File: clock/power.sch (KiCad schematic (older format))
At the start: 47 parts, among them U501 TPS56428, U502 TPS56428, U503 TPS56428

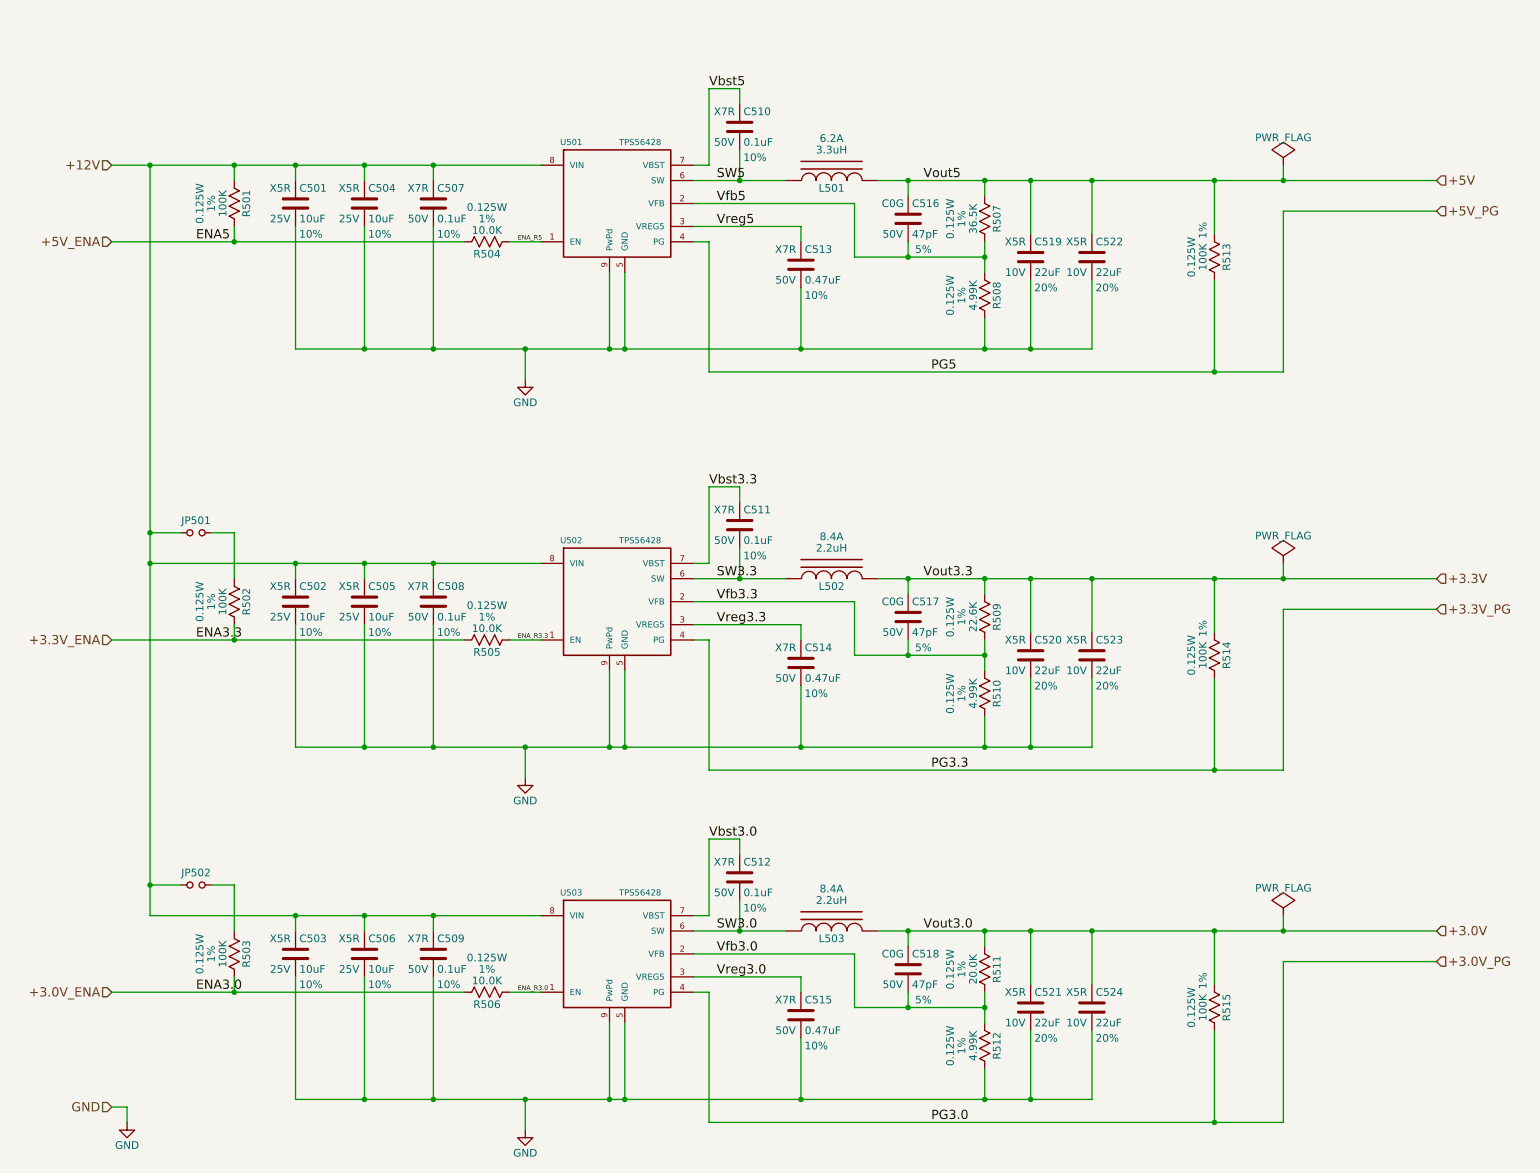
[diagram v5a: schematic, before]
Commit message: Preliminary changes from lab bring up.   Properly connect ref2 on PCA9306.   Duplicate +5V power good to drive +3.3V converter.   Change gain structure on OCXO control voltage drive.   Add FET control to disable linear regulators.
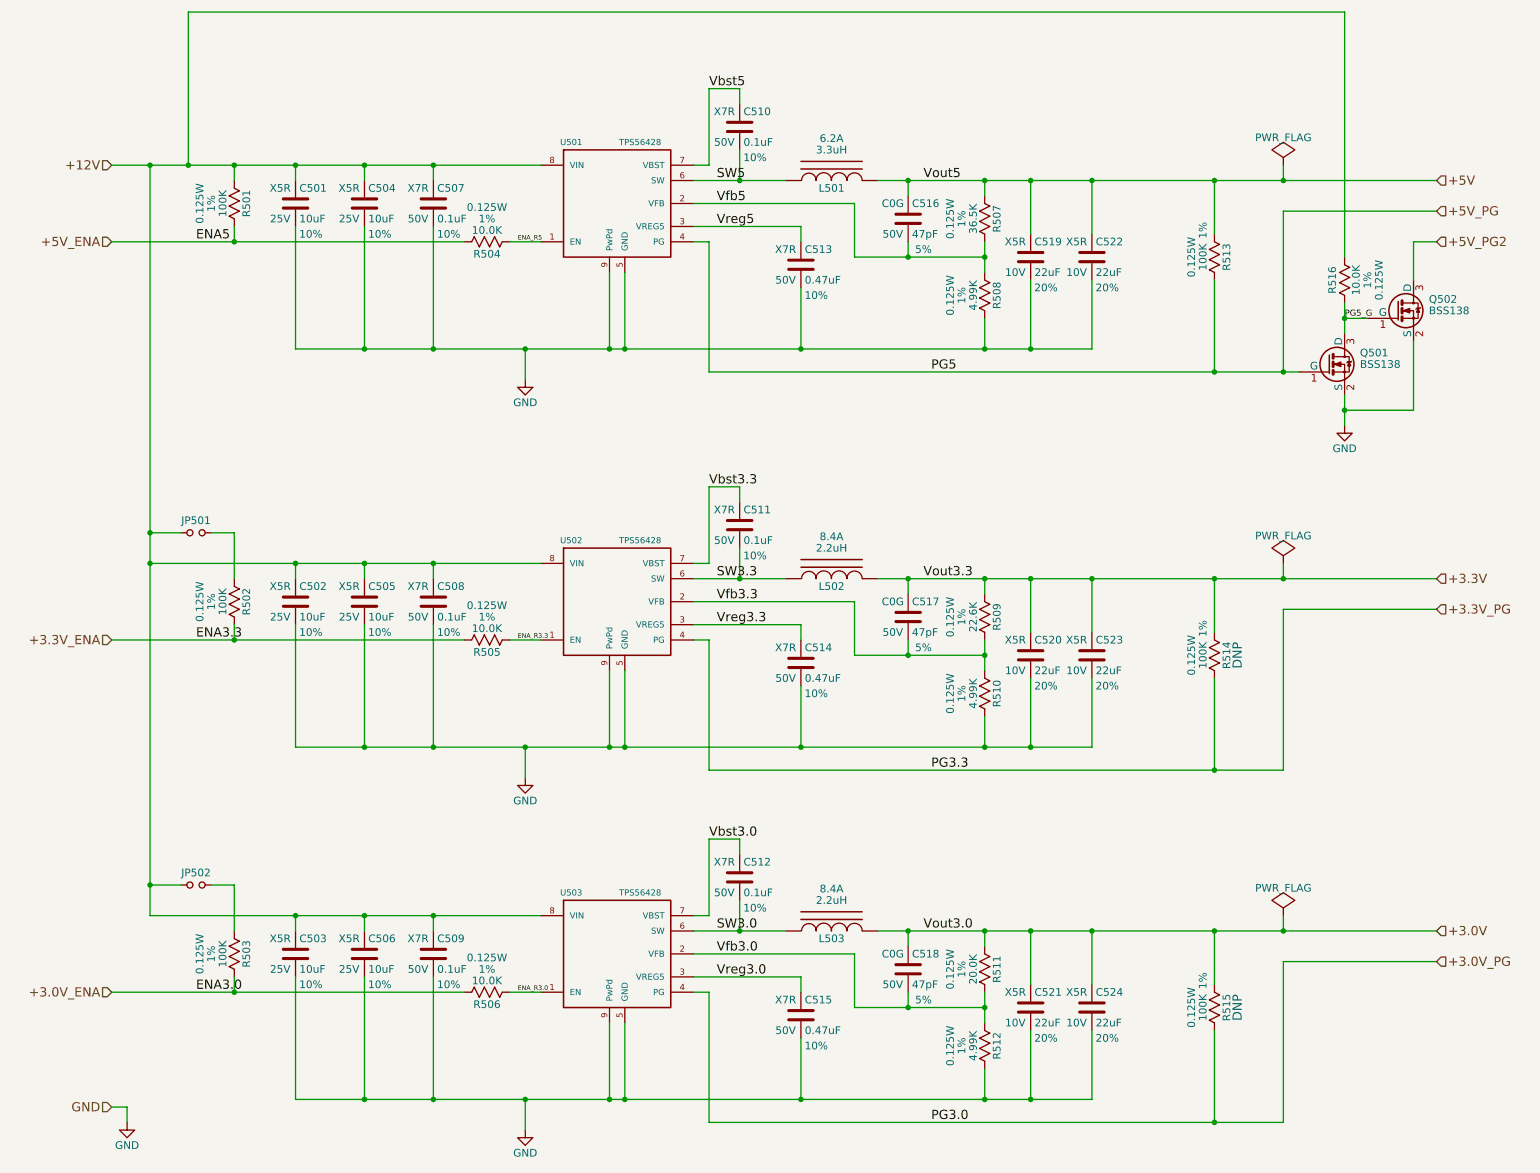
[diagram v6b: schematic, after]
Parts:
- added Q501, Q502: BSS138, local:SOT-23-3_NXP_HandSoldering, symbol BSS138
- added R516: 10.0K, Resistors_SMD:R_0805_HandSoldering, symbol R_local
- R514, R515: DNP (none) -> DNP
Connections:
- net +12V: now also R516.2
- net +5V_PG: now also Q501.1 (G)
- net GND: now also Q501.2 (S), Q502.2 (S)
- new net +5V_PG2: Q502.3 (D)
- new net PG5_G: Q501.3 (D), Q502.1 (G), R516.1
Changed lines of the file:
@@
 	3500 2750 5800 2750
 Wire Wire Line
-	7400 3600 11150 3600
+	7400 3600 11250 3600
 Wire Wire Line
 	6850 3450 6850 2950
@@
 Connection ~ 4300 2750
 $Comp
-L GND #PWR071
+L GND #PWR502
 U 1 1 55FF67B4
 P 6200 3650
-F 0 "#PWR071" H 6200 3400 50  0001 C CNN
+F 0 "#PWR502" H 6200 3400 50  0001 C CNN
 F 1 "GND" H 6200 3500 50  0000 C CNN
 F 2 "" H 6200 3650 60  0000 C CNN
@@
 Connection ~ 4300 5350
 $Comp
-L GND #PWR072
+L GND #PWR503
 U 1 1 5619E4B9
 P 6200 6250
-F 0 "#PWR072" H 6200 6000 50  0001 C CNN
+F 0 "#PWR503" H 6200 6000 50  0001 C CNN
 F 1 "GND" H 6200 6100 50  0000 C CNN
 F 2 "" H 6200 6250 60  0000 C CNN
@@
 Connection ~ 4300 7650
 $Comp
-L GND #PWR073
+L GND #PWR504
 U 1 1 561A0FCA
 P 6200 8550
-F 0 "#PWR073" H 6200 8300 50  0001 C CNN
+F 0 "#PWR504" H 6200 8300 50  0001 C CNN
 F 1 "GND" H 6200 8400 50  0000 C CNN
 F 2 "" H 6200 8550 60  0000 C CNN
@@
 F 6 "Vishay Dale" V 10700 5450 50  0001 C CNN "Manufacturer"
 F 7 "CRCW0805100KFKEA" V 10850 5450 50  0001 C CNN "PartNum"
+F 8 "DNP" V 10850 5450 60  0000 C CNN "DNP"
 	1    10700 5450
 	1    0    0    -1
@@
 F 6 "Vishay Dale" V 10700 7750 50  0001 C CNN "Manufacturer"
 F 7 "CRCW0805100KFKEA" V 10850 7750 50  0001 C CNN "PartNum"
+F 8 "DNP" V 10850 7750 60  0000 C CNN "DNP"
 	1    10700 7750
 	1    0    0    -1
@@
 GND
 $Comp
-L GND #PWR074
+L GND #PWR501
 U 1 1 563D8E93
 P 3600 8500
-F 0 "#PWR074" H 3600 8250 50  0001 C CNN
+F 0 "#PWR501" H 3600 8250 50  0001 C CNN
 F 1 "GND" H 3600 8350 50  0000 C CNN
 F 2 "" H 3600 8500 60  0000 C CNN
@@
 	3600 8400 3500 8400
 $Comp
-L PWR_FLAG #FLG075
+L PWR_FLAG #FLG501
 U 1 1 56439BF3
 P 11150 2250
-F 0 "#FLG075" H 11150 2345 50  0001 C CNN
+F 0 "#FLG501" H 11150 2345 50  0001 C CNN
 F 1 "PWR_FLAG" H 11150 2430 50  0000 C CNN
 F 2 "" H 11150 2250 60  0000 C CNN
@@
 Connection ~ 11150 2350
 $Comp
-L PWR_FLAG #FLG076
+L PWR_FLAG #FLG502
 U 1 1 5643A4B3
 P 11150 4850
-F 0 "#FLG076" H 11150 4945 50  0001 C CNN
+F 0 "#FLG502" H 11150 4945 50  0001 C CNN
 F 1 "PWR_FLAG" H 11150 5030 50  0000 C CNN
 F 2 "" H 11150 4850 60  0000 C CNN
@@
 Connection ~ 11150 4950
 $Comp
-L PWR_FLAG #FLG077
+L PWR_FLAG #FLG503
 U 1 1 5643AC28
 P 11150 7150
-F 0 "#FLG077" H 11150 7245 50  0001 C CNN
+F 0 "#FLG503" H 11150 7245 50  0001 C CNN
 F 1 "PWR_FLAG" H 11150 7330 50  0000 C CNN
 F 2 "" H 11150 7150 60  0000 C CNN
@@
 Wire Wire Line
 	4700 3450 9900 3450
+$Comp
+L BSS138 Q501
+U 1 1 57A96588
+P 11450 3550
+F 0 "Q501" H 11650 3625 50  0000 L CNN
+F 1 "BSS138" H 11650 3550 50  0000 L CNN
+F 2 "local:SOT-23-3_NXP_HandSoldering" H 11650 3475 50  0001 L CIN
+F 3 "" H 11450 3550 50  0000 L CNN
+F 4 "ON Semiconductor" H 11450 3550 60  0001 C CNN "Manufacturer"
+F 5 "BSS138LT1G" H 11450 3550 60  0001 C CNN "PartNum"
+	1    11450 3550
+	1    0    0    -1
+$EndComp
+$Comp
+L BSS138 Q502
+U 1 1 57A97046
+P 11900 3200
+F 0 "Q502" H 12100 3275 50  0000 L CNN
+F 1 "BSS138" H 12100 3200 50  0000 L CNN
+F 2 "local:SOT-23-3_NXP_HandSoldering" H 12100 3125 50  0001 L CIN
+F 3 "" H 11900 3200 50  0000 L CNN
+F 4 "ON Semiconductor" H 11900 3200 60  0001 C CNN "Manufacturer"
+F 5 "BSS138LT1G" H 11900 3200 60  0001 C CNN "PartNum"
+	1    11900 3200
+	1    0    0    -1
+$EndComp
+Text HLabel 12150 2750 2    60   Input ~ 0
++5V_PG2
+$Comp
+L R_local R516
+U 1 1 57A9749D
+P 11550 3000
+F 0 "R516" V 11630 3000 50  0000 C CNN
+F 1 "10.0K" V 11475 3000 50  0000 C CNN
+F 2 "Resistors_SMD:R_0805_HandSoldering" V 11480 3000 30  0001 C CNN
+F 3 "" V 11630 3000 30  0000 C CNN
+F 4 "1%" V 11400 3000 50  0000 C CNN "Tolerance"
+F 5 "0.125W" V 11325 3000 50  0000 C CNN "Power"
+F 6 "Vishay Dale" V 11550 3000 50  0001 C CNN "Manufacturer"
+F 7 "CRCW080510K0FKEA" V 11700 3000 50  0001 C CNN "PartNum"
+	1    11550 3000
+	-1   0    0    1
+$EndComp
+Wire Wire Line
+	11550 3150 11550 3350
+Wire Wire Line
+	11700 3250 11550 3250
+Connection ~ 11550 3250
+Wire Wire Line
+	12000 3400 12000 3850
+Wire Wire Line
+	12000 3850 11550 3850
+Wire Wire Line
+	11550 3750 11550 3950
+$Comp
+L GND #PWR505
+U 1 1 57A97EAC
+P 11550 3950
+F 0 "#PWR505" H 11550 3700 50  0001 C CNN
+F 1 "GND" H 11550 3800 50  0000 C CNN
+F 2 "" H 11550 3950 60  0000 C CNN
+F 3 "" H 11550 3950 60  0000 C CNN
+	1    11550 3950
+	1    0    0    -1
+$EndComp
+Connection ~ 11550 3850
+Connection ~ 11150 3600
+Wire Wire Line
+	12000 3000 12000 2750
+Wire Wire Line
+	12000 2750 12150 2750
+Wire Wire Line
+	11550 2850 11550 1250
+Wire Wire Line
+	11550 1250 4000 1250
+Wire Wire Line
+	4000 1250 4000 2250
+Connection ~ 4000 2250
+Text Label 11550 3250 0    40   ~ 0
+PG5_G
 $EndSCHEMATC
